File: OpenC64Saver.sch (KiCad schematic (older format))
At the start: 15 parts, among them J1 Power I/O, Q1 PN2222A, Q2 PN2222A

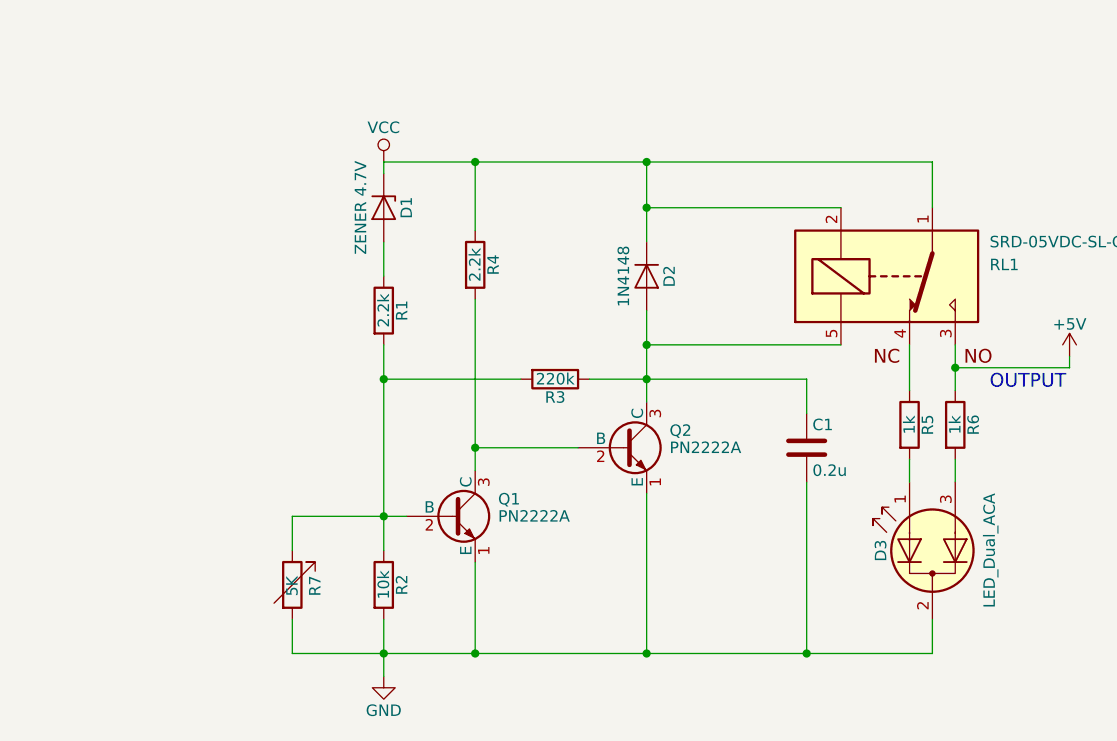
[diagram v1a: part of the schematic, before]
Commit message: Remove R2, decrease R1 (and add note. The variable resistor is usually enough. It was R7, it is now R2.
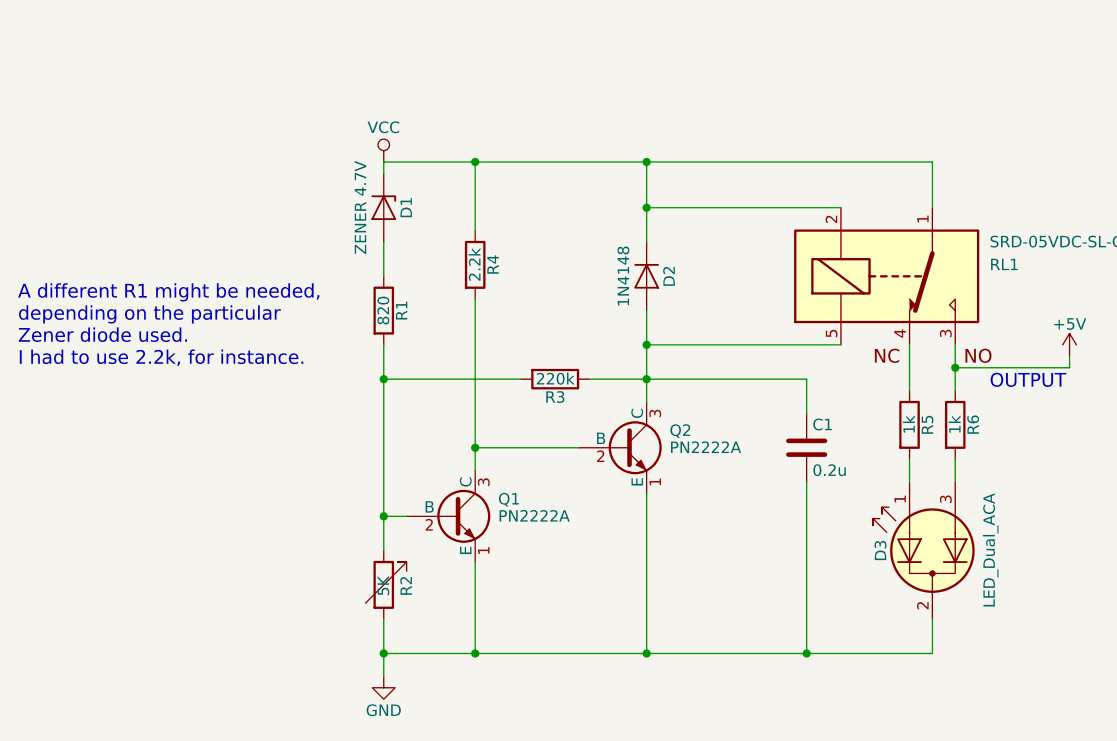
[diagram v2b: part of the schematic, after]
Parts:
- removed R2: 10k, Resistors_SMD:R_0805_HandSoldering, symbol R
- R1: value 2.2k -> 820
- renumbered R7 to R2
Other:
- note added: "A different R1 might be needed,\ndepending on the particular\nZener diode used.\nI had to use 2.2k, for instance."
- moved on the sheet: R2
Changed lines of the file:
@@
 LIBS:valves
 LIBS:relays
-LIBS:Sukko
-LIBS:C64Saver-cache
+LIBS:OpenC64Saver-cache
 EELAYER 25 0
 EELAYER END
@@
 $EndComp
 $Comp
-L R R2
-U 1 1 59765DBB
-P 4200 3200
-F 0 "R2" V 4280 3200 50  0000 C CNN
-F 1 "10k" V 4200 3200 50  0000 C CNN
-F 2 "Resistors_SMD:R_0805_HandSoldering" V 4130 3200 50  0001 C CNN
-F 3 "" H 4200 3200 50  0000 C CNN
-	1    4200 3200
-	1    0    0    -1
-$EndComp
-$Comp
 L GND #PWR01
 U 1 1 59765E30
@@
 P 4200 2000
 F 0 "R1" V 4280 2000 50  0000 C CNN
-F 1 "2.2k" V 4200 2000 50  0000 C CNN
+F 1 "820" V 4200 2000 50  0000 C CNN
 F 2 "Resistors_SMD:R_0805_HandSoldering" V 4130 2000 50  0001 C CNN
 F 3 "" H 4200 2000 50  0000 C CNN
@@
 $EndComp
 Wire Wire Line
-	4200 2150 4200 3050
-Wire Wire Line
-	3800 2900 4300 2900
-Wire Wire Line
-	4200 3350 4200 3600
-Wire Wire Line
-	3800 3500 6600 3500
+	4200 2150 4200 2300
+Wire Wire Line
+	4200 2300 4200 2900
+Wire Wire Line
+	4200 2900 4300 2900
+Wire Wire Line
+	4200 3500 4200 3600
+Wire Wire Line
+	4200 3500 4600 3500
+Wire Wire Line
+	4600 3500 5350 3500
+Wire Wire Line
+	5350 3500 6050 3500
+Wire Wire Line
+	6050 3500 6600 3500
 Wire Wire Line
 	4600 3500 4600 3100
 Connection ~ 4200 2900
 Wire Wire Line
-	4600 1950 4600 2700
+	4600 1950 4600 2600
+Wire Wire Line
+	4600 2600 4600 2700
 Wire Wire Line
 	4600 2600 5050 2600
@@
 Connection ~ 4600 3500
 Wire Wire Line
-	5350 2000 5350 2400
+	5350 2000 5350 2150
+Wire Wire Line
+	5350 2150 5350 2300
+Wire Wire Line
+	5350 2300 5350 2400
 Connection ~ 4200 2300
 Wire Wire Line
-	5100 2300 6050 2300
+	5100 2300 5350 2300
+Wire Wire Line
+	5350 2300 6050 2300
 Wire Wire Line
 	4200 2300 4800 2300
@@
 Connection ~ 5350 3500
 Wire Wire Line
-	5350 1350 5350 1700
-Wire Wire Line
-	4200 1350 6600 1350
+	5350 1350 5350 1550
+Wire Wire Line
+	5350 1550 5350 1700
+Wire Wire Line
+	4200 1350 4600 1350
+Wire Wire Line
+	4600 1350 5350 1350
+Wire Wire Line
+	5350 1350 6600 1350
 Wire Wire Line
 	4200 1350 4200 1400
@@
 $EndComp
 Wire Wire Line
-	6700 2150 6700 2350
+	6700 2150 6700 2250
+Wire Wire Line
+	6700 2250 6700 2350
 Wire Wire Line
 	6700 2250 7200 2250
@@
 	6700 2650 6700 2750
 Connection ~ 6700 2250
-$Comp
-L R_Variable R7
-U 1 1 59768CBA
-P 3800 3200
-F 0 "R7" V 3900 3150 50  0000 L CNN
-F 1 "5K" V 3800 3150 50  0000 L CNN
-F 2 "pth_resistors:trimmer_vishay_64w" V 3730 3200 50  0001 C CNN
-F 3 "" H 3800 3200 50  0000 C CNN
-	1    3800 3200
-	1    0    0    -1
-$EndComp
-Wire Wire Line
-	3800 2900 3800 3050
-Wire Wire Line
-	3800 3350 3800 3500
 Connection ~ 4200 3500
 Wire Wire Line
@@
 Text Notes 6850 2350 0    60   ~ 0
 OUTPUT
+$Comp
+L R_Variable R2
+U 1 1 59768CBA
+P 4200 3200
+F 0 "R2" V 4300 3150 50  0000 L CNN
+F 1 "5K" V 4200 3150 50  0000 L CNN
+F 2 "pth_resistors:trimmer_vishay_64w" V 4130 3200 50  0001 C CNN
+F 3 "" H 4200 3200 50  0000 C CNN
+	1    4200 3200
+	1    0    0    -1
+$EndComp
+Wire Wire Line
+	4200 3350 4200 3500
+Wire Wire Line
+	4200 2900 4200 3050
+Text Notes 2600 2250 0    60   ~ 0
+A different R1 might be needed,\ndepending on the particular\nZener diode used.\nI had to use 2.2k, for instance.
 $EndSCHEMATC

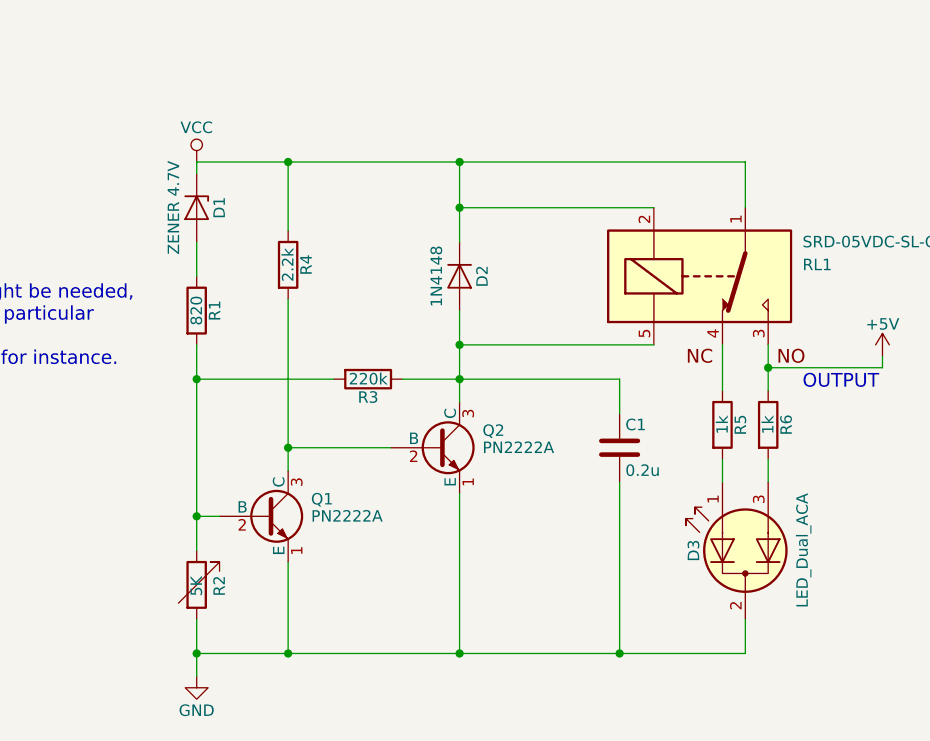
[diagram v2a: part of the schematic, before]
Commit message: Rotate R2 to reorient silkscreen on PCB
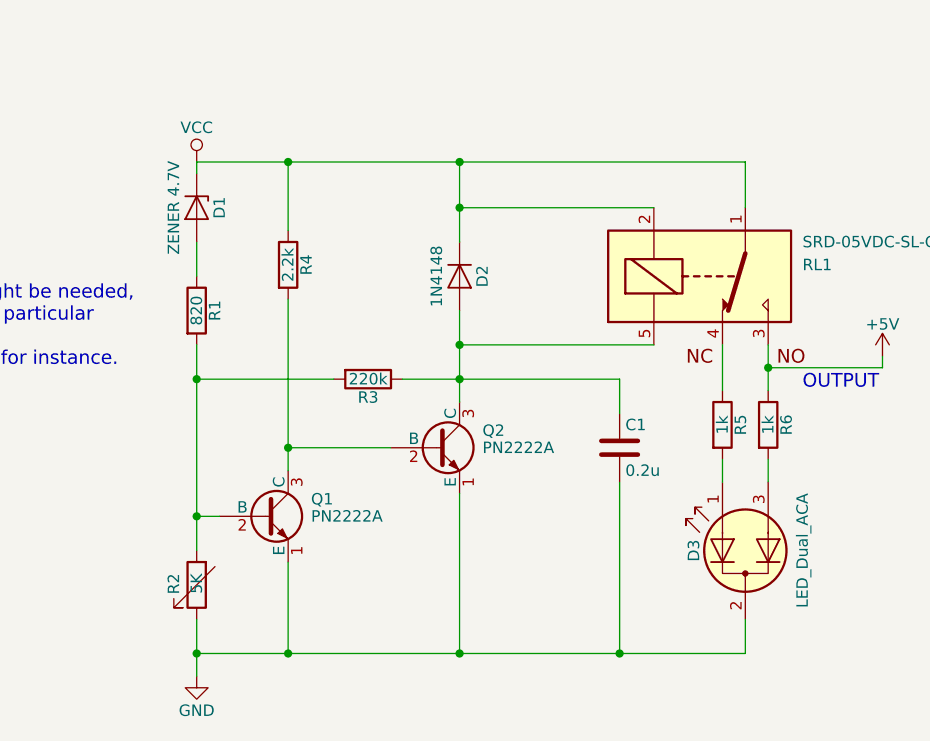
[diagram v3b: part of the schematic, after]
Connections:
- net GND: now also R2.1; no longer R2.2
- net at Q1.2 (B), R1.2, R3.2: now also R2.2; no longer R2.1
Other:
- moved on the sheet: R2
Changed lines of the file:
@@
 $EndComp
 Wire Wire Line
-	4200 2150 4200 2300
-Wire Wire Line
-	4200 2300 4200 2900
+	4200 2150 4200 3050
 Wire Wire Line
 	4200 2900 4300 2900
 Wire Wire Line
-	4200 3500 4200 3600
-Wire Wire Line
-	4200 3500 4600 3500
-Wire Wire Line
-	4600 3500 5350 3500
-Wire Wire Line
-	5350 3500 6050 3500
-Wire Wire Line
-	6050 3500 6600 3500
+	4200 3350 4200 3600
+Wire Wire Line
+	4200 3500 6600 3500
 Wire Wire Line
 	4600 3500 4600 3100
 Connection ~ 4200 2900
 Wire Wire Line
-	4600 1950 4600 2600
-Wire Wire Line
-	4600 2600 4600 2700
+	4600 1950 4600 2700
 Wire Wire Line
 	4600 2600 5050 2600
@@
 Connection ~ 4600 3500
 Wire Wire Line
-	5350 2000 5350 2150
-Wire Wire Line
-	5350 2150 5350 2300
-Wire Wire Line
-	5350 2300 5350 2400
+	5350 2000 5350 2400
 Connection ~ 4200 2300
 Wire Wire Line
-	5100 2300 5350 2300
-Wire Wire Line
-	5350 2300 6050 2300
+	5100 2300 6050 2300
 Wire Wire Line
 	4200 2300 4800 2300
@@
 Connection ~ 5350 3500
 Wire Wire Line
-	5350 1350 5350 1550
-Wire Wire Line
-	5350 1550 5350 1700
-Wire Wire Line
-	4200 1350 4600 1350
-Wire Wire Line
-	4600 1350 5350 1350
-Wire Wire Line
-	5350 1350 6600 1350
+	5350 1350 5350 1700
+Wire Wire Line
+	4200 1350 6600 1350
 Wire Wire Line
 	4200 1350 4200 1400
@@
 $EndComp
 Wire Wire Line
-	6700 2150 6700 2250
-Wire Wire Line
-	6700 2250 6700 2350
+	6700 2150 6700 2350
 Wire Wire Line
 	6700 2250 7200 2250
@@
 F 3 "" H 4200 3200 50  0000 C CNN
 	1    4200 3200
-	1    0    0    -1
-$EndComp
-Wire Wire Line
-	4200 3350 4200 3500
-Wire Wire Line
-	4200 2900 4200 3050
+	-1   0    0    1
+$EndComp
 Text Notes 2600 2250 0    60   ~ 0
 A different R1 might be needed,\ndepending on the particular\nZener diode used.\nI had to use 2.2k, for instance.

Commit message: Remove R2 and reorient trimmer (which is now R2)
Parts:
- added X1: OSHW_LOGO, w_logo:Logo_copper_OSHW_6x6mm, symbol CONN_01X01
- added X2: SCREW_HOLE, Connectors:1pin, symbol CONN_01X01
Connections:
- net GND: now also R2.2; no longer R2.1
- net at Q1.2 (B), R1.2, R3.2: now also R2.1; no longer R2.2
- no-connect marks 0 -> 2
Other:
- moved on the sheet: R2
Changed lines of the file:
@@
 F 3 "" H 4200 3200 50  0000 C CNN
 	1    4200 3200
-	-1   0    0    1
+	1    0    0    -1
 $EndComp
 Text Notes 2600 2250 0    60   ~ 0
 A different R1 might be needed,\ndepending on the particular\nZener diode used.\nI had to use 2.2k, for instance.
+$Comp
+L CONN_01X01 X2
+U 1 1 59D9407F
+P 10900 6300
+F 0 "X2" H 10900 6400 50  0000 C CNN
+F 1 "SCREW_HOLE" V 11000 6300 50  0000 C CNN
+F 2 "Connectors:1pin" H 10900 6300 50  0001 C CNN
+F 3 "" H 10900 6300 50  0001 C CNN
+	1    10900 6300
+	0    1    1    0
+$EndComp
+$Comp
+L CONN_01X01 X1
+U 1 1 59D9413E
+P 10400 6300
+F 0 "X1" H 10400 6400 50  0000 C CNN
+F 1 "OSHW_LOGO" V 10500 6300 50  0000 C CNN
+F 2 "w_logo:Logo_copper_OSHW_6x6mm" H 10400 6300 50  0001 C CNN
+F 3 "" H 10400 6300 50  0001 C CNN
+	1    10400 6300
+	0    1    1    0
+$EndComp
+NoConn ~ 10400 6100
+NoConn ~ 10900 6100
 $EndSCHEMATC

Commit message: Fit a 2nd screw hole
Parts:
- added X3: SCREW_HOLE, Connectors:1pin, symbol CONN_01X01
- R2: footprint pth_resistors:trimmer_vishay_64w -> C64Saver:trimmer_vishay_64w
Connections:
- no-connect marks 2 -> 3
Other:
- moved on the sheet: X1, X2
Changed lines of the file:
@@
 F 0 "R2" V 4300 3150 50  0000 L CNN
 F 1 "5K" V 4200 3150 50  0000 L CNN
-F 2 "pth_resistors:trimmer_vishay_64w" V 4130 3200 50  0001 C CNN
+F 2 "C64Saver:trimmer_vishay_64w" V 4130 3200 50  0001 C CNN
 F 3 "" H 4200 3200 50  0000 C CNN
 	1    4200 3200
@@
 L CONN_01X01 X2
 U 1 1 59D9407F
+P 10400 6300
+F 0 "X2" H 10400 6400 50  0000 C CNN
+F 1 "SCREW_HOLE" V 10500 6300 50  0000 C CNN
+F 2 "Connectors:1pin" H 10400 6300 50  0001 C CNN
+F 3 "" H 10400 6300 50  0001 C CNN
+	1    10400 6300
+	0    1    1    0
+$EndComp
+$Comp
+L CONN_01X01 X1
+U 1 1 59D9413E
+P 9900 6300
+F 0 "X1" H 9900 6400 50  0000 C CNN
+F 1 "OSHW_LOGO" V 10000 6300 50  0000 C CNN
+F 2 "w_logo:Logo_copper_OSHW_6x6mm" H 9900 6300 50  0001 C CNN
+F 3 "" H 9900 6300 50  0001 C CNN
+	1    9900 6300
+	0    1    1    0
+$EndComp
+NoConn ~ 9900 6100
+NoConn ~ 10400 6100
+$Comp
+L CONN_01X01 X3
+U 1 1 59D94B0F
 P 10900 6300
-F 0 "X2" H 10900 6400 50  0000 C CNN
+F 0 "X3" H 10900 6400 50  0000 C CNN
 F 1 "SCREW_HOLE" V 11000 6300 50  0000 C CNN
 F 2 "Connectors:1pin" H 10900 6300 50  0001 C CNN
@@
 	0    1    1    0
 $EndComp
-$Comp
-L CONN_01X01 X1
-U 1 1 59D9413E
-P 10400 6300
-F 0 "X1" H 10400 6400 50  0000 C CNN
-F 1 "OSHW_LOGO" V 10500 6300 50  0000 C CNN
-F 2 "w_logo:Logo_copper_OSHW_6x6mm" H 10400 6300 50  0001 C CNN
-F 3 "" H 10400 6300 50  0001 C CNN
-	1    10400 6300
-	0    1    1    0
-$EndComp
-NoConn ~ 10400 6100
 NoConn ~ 10900 6100
 $EndSCHEMATC
